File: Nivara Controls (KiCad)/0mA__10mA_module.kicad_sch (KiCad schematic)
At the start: 5 parts, among them U3 GP8201-SOP8

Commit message: Actualizado
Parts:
- removed U3: GP8201-SOP8, EastEDA:SOP-8_L4.9-W3.9-P1.27-LS6.0-BL, symbol EDA:GP8201-SOP8
- added R20, R21: R_0603, PCM_Resistor_SMD_AKL:R_0603_1608Metric, symbol PCM_Resistor_US_AKL:R_0603
- added U5: GP8201S-TC50-EW, EasyEDA:ESOP-8_L4.9-W3.9-P1.27-LS6.0-BL-EP, symbol EDA:GP8201S-TC50-EW
- C15, C16: Voltaje 10v -> (none)
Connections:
- net GND: now also C15.1, D7.2 (A), U5.5 (GND)
- net SCLK: now also R20.1, U5.1 (SCLK)
- net SDA: now also R21.1, U5.2 (SDA)
- net VCC: now also U5.4 (VCC)
- net A_Out: now reaches C15.2, D7.1 (K)
- net A_Out: now also U5.6 (VOUT)
- net at C16.1, R15.2: now also U5.8 (V5V)
- net SEL: no longer names the net of R15.1
- net SEL: now also U5.7 (SEL)
- new net +3.3V: R20.2, R21.2
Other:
- moved on the sheet: C16

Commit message: Trabajando en PCB
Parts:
- U5: footprint EasyEDA:ESOP-8_L4.9-W3.9-P1.27-LS6.0-BL-EP -> EastEDA:GP8303-TC50-EW
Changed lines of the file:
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@@
 			)
 		)
-		(property "Footprint" "EasyEDA:ESOP-8_L4.9-W3.9-P1.27-LS6.0-BL-EP"
+		(property "Footprint" "EastEDA:GP8303-TC50-EW"
 			(at 120.65 80.01 0)
 			(effects

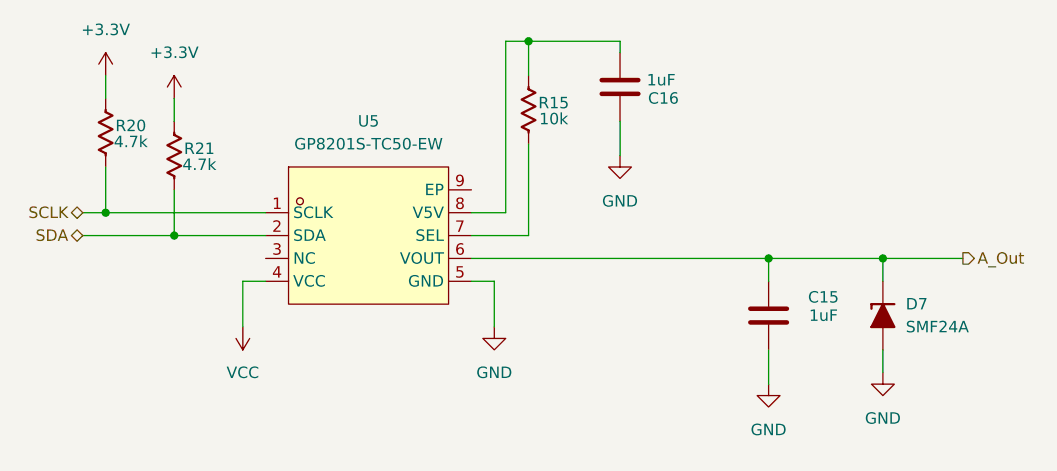
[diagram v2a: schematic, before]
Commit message: Actualizació Orden de componentes
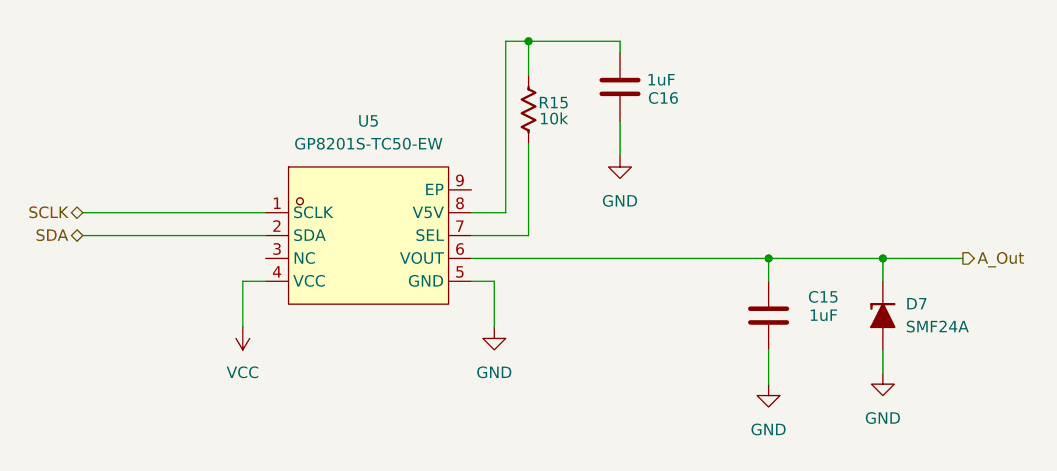
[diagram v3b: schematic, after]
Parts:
- removed R20, R21: R_0603, PCM_Resistor_SMD_AKL:R_0603_1608Metric, symbol PCM_Resistor_US_AKL:R_0603
